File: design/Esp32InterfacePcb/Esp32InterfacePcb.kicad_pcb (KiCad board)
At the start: 2 copper layers, 48.5 x 31.6 mm, 14 parts, among them J1 Conn_01x02, J3 Conn_01x03, J4 Conn_01x10, J5 Conn_01x10, J6 Conn_01x10, J7 Conn_01x10, SW1 EN, SW2 IO0, U1 ESP32-WROOM-E

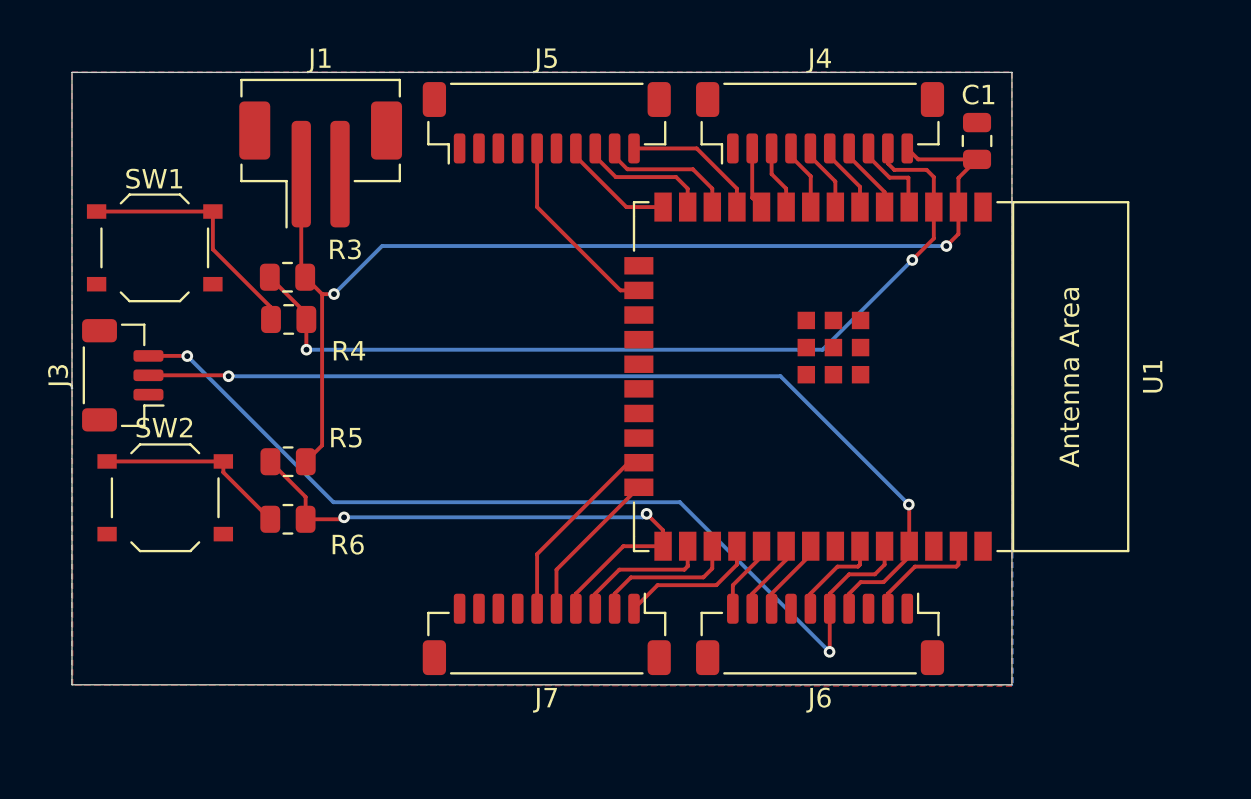
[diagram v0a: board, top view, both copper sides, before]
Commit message: best adaptation to adafruit swirly grill
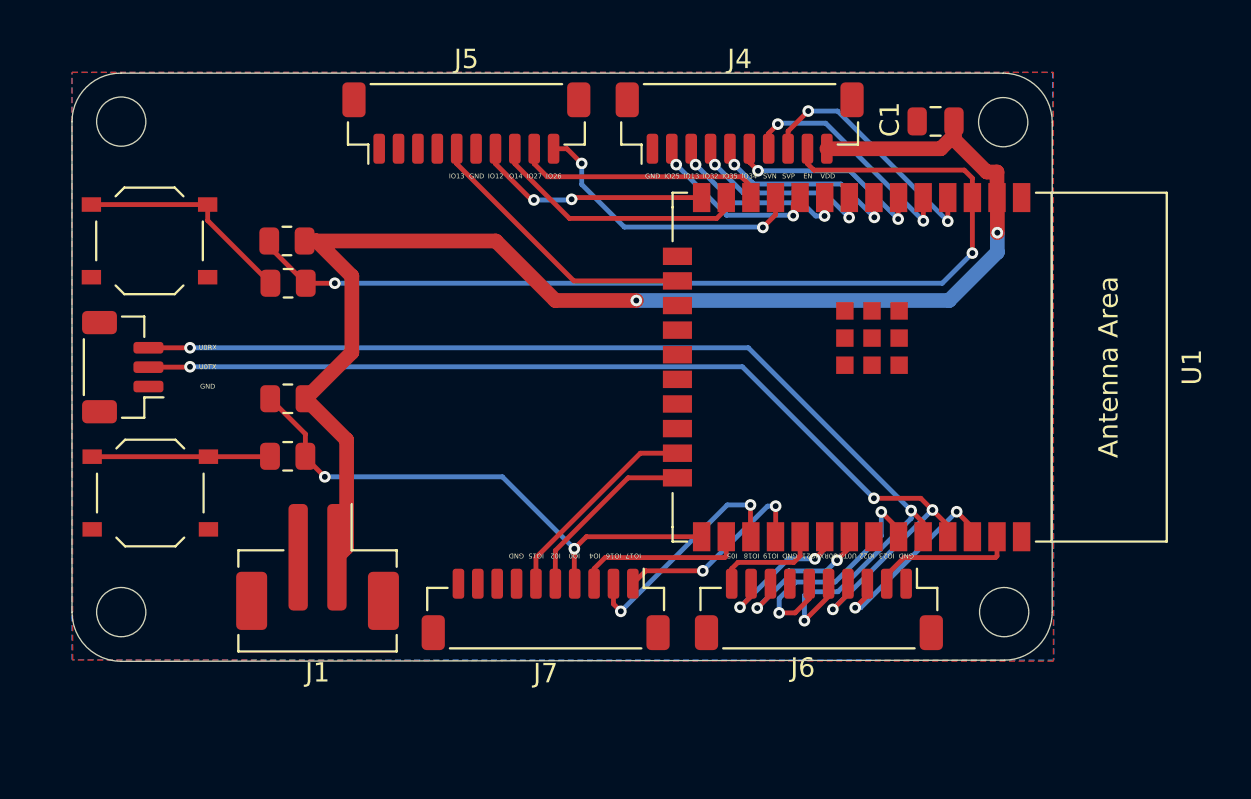
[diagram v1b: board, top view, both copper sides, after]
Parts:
- moved J1 20.8 mm to (47.7, 60.5), turned to 180 degrees
- moved J5 4.15 mm to (55.4, 37.6)
- moved J4 4.15 mm to (69.5, 37.6)
- moved R5 3.25 mm to (46.1, 51.8)
- moved R6 3.25 mm to (46.1, 54.8)
- moved C1 2.37 mm to (79.6, 37.5), turned to 180 degrees
- moved U1 2.05 mm to (77.0, 50.2)
- moved R3 1.87 mm to (46.1, 43.7)
- moved R4 1.87 mm to (46.1, 45.9)
- moved J7 1.29 mm to (59.4, 62.7)
- moved J6 1.29 mm to (73.5, 62.7)
- moved SW2 0.81 mm to (39.0, 56.7)
- moved SW1 0.45 mm to (39.0, 43.7)
- moved J3 0.42 mm to (37.6, 50.2)
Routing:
- net VDD: track 57.8 -> 73.4 mm
- net IO22: track 0.00 -> 10.4 mm, vias 0 -> 2
- net SVP: track 4.46 -> 13.2 mm, vias 0 -> 2
- net SVN: track 3.78 -> 12.3 mm, vias 0 -> 2
- net IO21: track 4.91 -> 12.9 mm, vias 0 -> 2
- net IO26: track 7.12 -> 14.9 mm, vias 0 -> 2
- net IO34: track 3.67 -> 10.7 mm, vias 0 -> 2
- net UORX: track 48.9 -> 55.7 mm, vias 2 -> 3
- net IO14: track 6.82 -> 13.6 mm
- net IO35: track 3.56 -> 10.4 mm, vias 0 -> 2
- net IO32: track 3.45 -> 10.0 mm, vias 0 -> 2
- net IO33: track 3.34 -> 9.62 mm, vias 0 -> 2
- net IO12: track 6.00 -> 12.2 mm, vias 0 -> 2
- net IO27: track 7.09 -> 13.0 mm
- net IO25: track 3.22 -> 9.13 mm, vias 0 -> 2
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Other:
- board size 48.5 x 31.6 mm -> 50.6 x 30.3 mm
- board text added: "EN"
- board text added: "GND"
- board text added: "I02"
- board text added: "I05"
- board text added: "IO0"
- board text added: "IO12"
- board text added: "IO13"
- board text added: "IO14"
- board text added: "IO15"
- board text added: "IO16"
- board text added: "IO17"
- board text added: "IO18"
- board text added: "IO19"
- board text added: "IO21"
- board text added: "IO22"
- board text added: "IO23"
- board text added: "IO25"
- board text added: "IO26"
- board text added: "IO27"
- board text added: "IO32"
- board text added: "IO34"
- board text added: "IO35"
- board text added: "IO4"
- board text added: "SVN"
- board text added: "SVP"
- board text added: "U0RX"
- board text added: "U0TX"
- board text added: "VDD"

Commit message: adjustement and gerber files
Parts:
- C1: value 100uF -> 100nF; footprint Capacitor_SMD:C_0805_2012Metric -> Capacitor_SMD:C_0603_1608Metric_Pad1.08x0.95mm_HandSolder
- J1: footprint Connector_JST:JST_PH_B2B-PH-SM4-TB_1x02-1MP_P2.00mm_Vertical -> Connector_JST:JST_PH_S2B-PH-SM4-TB_1x02-1MP_P2.00mm_Horizontal
- J3: footprint Connector_JST:JST_SH_BM03B-SRSS-TB_1x03-1MP_P1.00mm_Vertical -> Connector_JST:JST_SH_SM03B-SRSS-TB_1x03-1MP_P1.00mm_Horizontal
- J4, J5, J6, J7: footprint Connector_JST:JST_SH_BM10B-SRSS-TB_1x10-1MP_P1.00mm_Vertical -> Connector_JST:JST_SH_SM10B-SRSS-TB_1x10-1MP_P1.00mm_Horizontal
- R3, R4, R5, R6: footprint Resistor_SMD:R_0805_2012Metric -> Resistor_SMD:R_0603_1608Metric_Pad0.98x0.95mm_HandSolder
- moved R5 7.86 mm to (52.0, 57.1)
- moved R3 5.96 mm to (52.0, 44.5)
- moved J4 5.21 mm to (74.6, 38.3), turned to 180 degrees
- moved C1 5.10 mm to (83.3, 40.9), turned to 0 degrees
- moved J1 4.58 mm to (48.0, 65.1), turned to 0 degrees
- moved J6 4.48 mm to (74.5, 67.1), turned to 0 degrees
- moved J7 4.34 mm to (60.0, 67.0), turned to 0 degrees
- moved J3 2.86 mm to (39.0, 52.7), turned to -90 degrees
- moved SW1 2.84 mm to (39.5, 46.5)
- moved U1 2.49 mm to (77.0, 52.7)
- moved SW2 2.29 mm to (39.5, 59.0)
- moved R6 2.27 mm to (46.0, 57.1)
- moved J5 2.10 mm to (57.4, 38.0), turned to 180 degrees
- moved R4 1.37 mm to (46.0, 44.5)
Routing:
- net VDD: track 73.4 -> 57.3 mm
- net SVP: track 13.2 -> 5.47 mm, vias 2 -> 0
- net SVN: track 12.3 -> 5.32 mm, vias 2 -> 0
- net IO21: track 12.9 -> 5.92 mm, vias 2 -> 0
- net IO35: track 10.4 -> 4.55 mm, vias 2 -> 0
- net IO32: track 10.0 -> 4.44 mm, vias 2 -> 0
- net IO33: track 9.62 -> 4.33 mm, vias 2 -> 0
- net EN: track 51.5 -> 46.4 mm
- net IO25: track 9.13 -> 4.21 mm, vias 2 -> 0
- net IO26: track 14.9 -> 11.6 mm, vias 2 -> 0
- net IO16: track 12.2 -> 8.88 mm, vias 2 -> 0
- net GND: track 0.00 -> 3.10 mm
- net IO19: track 8.33 -> 5.33 mm, vias 2 -> 0
- net IO18: track 7.70 -> 4.82 mm, vias 2 -> 0
- net Net-(R4-Pad1): track 11.4 -> 8.60 mm
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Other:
- board size 50.6 x 30.3 mm -> 50.6 x 35.3 mm
- board text removed: "EN"
- board text removed: "GND"
- board text removed: "I02"
- board text removed: "I05"
- board text removed: "IO0"
- board text removed: "IO12"
- board text removed: "IO13"
- board text removed: "IO14"
- board text removed: "IO15"
- board text removed: "IO16"
- board text removed: "IO17"
- board text removed: "IO18"
- board text removed: "IO19"
- board text removed: "IO21"
- board text removed: "IO22"
- board text removed: "IO23"
- board text removed: "IO25"
- board text removed: "IO26"
- board text removed: "IO27"
- board text removed: "IO32"
- board text removed: "IO34"
- board text removed: "IO35"
- board text removed: "IO4"
- board text removed: "SVN"
- board text removed: "SVP"
- board text removed: "U0RX"
- board text removed: "U0TX"
- board text removed: "VDD"
